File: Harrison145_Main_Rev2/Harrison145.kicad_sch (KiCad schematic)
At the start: 0 parts

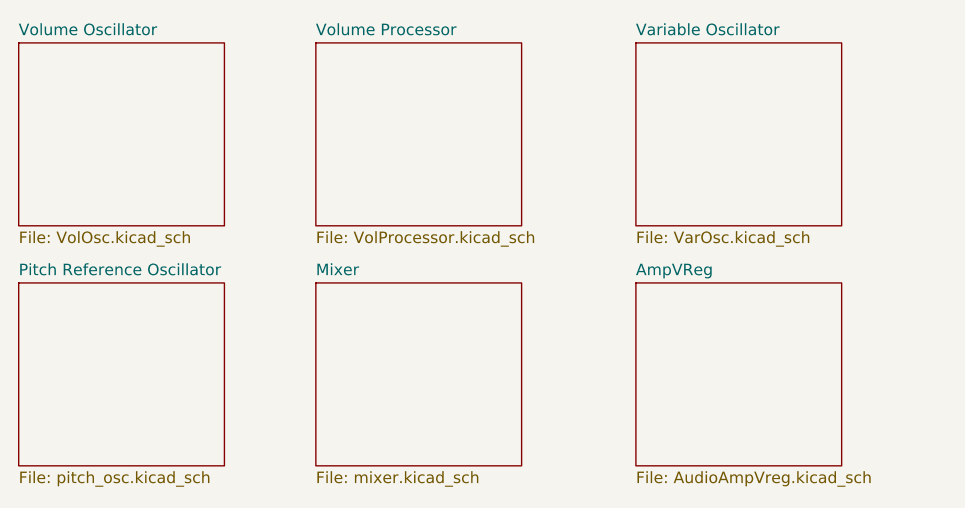
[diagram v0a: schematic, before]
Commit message: Remove kicad sims
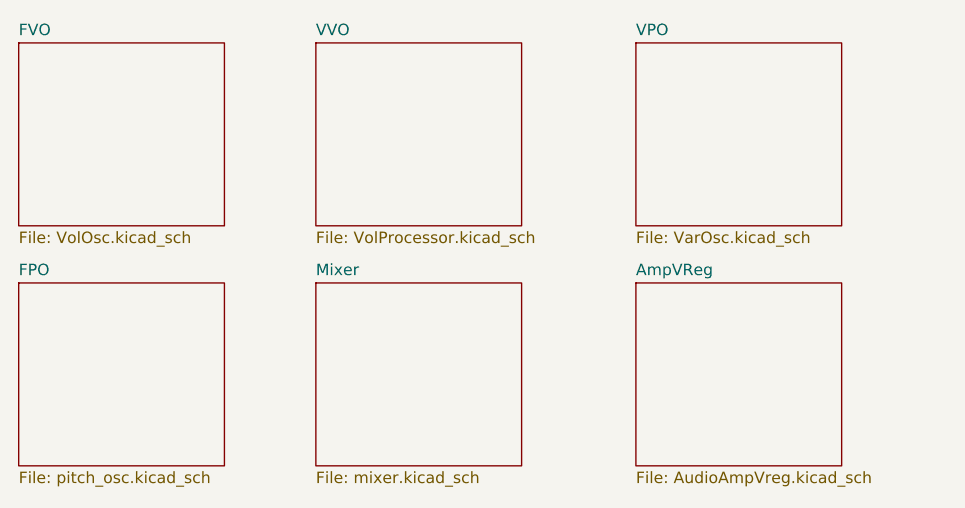
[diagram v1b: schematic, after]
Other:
- sheet Pitch Reference Oscillator renamed FPO
- sheet Variable Oscillator renamed VPO
- sheet Volume Oscillator renamed FVO
- sheet Volume Processor renamed VVO
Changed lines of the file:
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@@
     (stroke (width 0.1524) (type solid))
     (fill (color 0 0 0 0.0000))
-    (property "Sheetname" "Variable Oscillator" (at 180.34 76.7584 0)
+    (property "Sheetname" "VPO" (at 180.34 76.7584 0)
       (effects (font (size 1.27 1.27)) (justify left bottom))
     )
@@
     (stroke (width 0.1524) (type solid))
     (fill (color 0 0 0 0.0000))
-    (property "Sheetname" "Volume Processor" (at 144.78 76.7584 0)
+    (property "Sheetname" "VVO" (at 144.78 76.7584 0)
       (effects (font (size 1.27 1.27)) (justify left bottom))
     )
@@
     (stroke (width 0.1524) (type solid))
     (fill (color 0 0 0 0.0000))
-    (property "Sheetname" "Volume Oscillator" (at 111.76 76.7584 0)
+    (property "Sheetname" "FVO" (at 111.76 76.7584 0)
       (effects (font (size 1.27 1.27)) (justify left bottom))
     )
@@
     (stroke (width 0.1524) (type solid))
     (fill (color 0 0 0 0.0000))
-    (property "Sheetname" "Pitch Reference Oscillator" (at 111.76 103.4284 0)
+    (property "Sheetname" "FPO" (at 111.76 103.4284 0)
       (effects (font (size 1.27 1.27)) (justify left bottom))
     )
